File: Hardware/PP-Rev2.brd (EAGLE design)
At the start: 190.5 x 101.3 mm, 181 parts, among them IC1 LT6004, IC2 TLC6C5912-Q1, J1 J_0399700102, Q1 MOSFET-PCHANNEL, Q10 2N7002PW, Q11 2N7002PW, Q12 2N7002PW, Q13 2N7002PW, Q14 2N7002PW, Q15 2N7002PW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

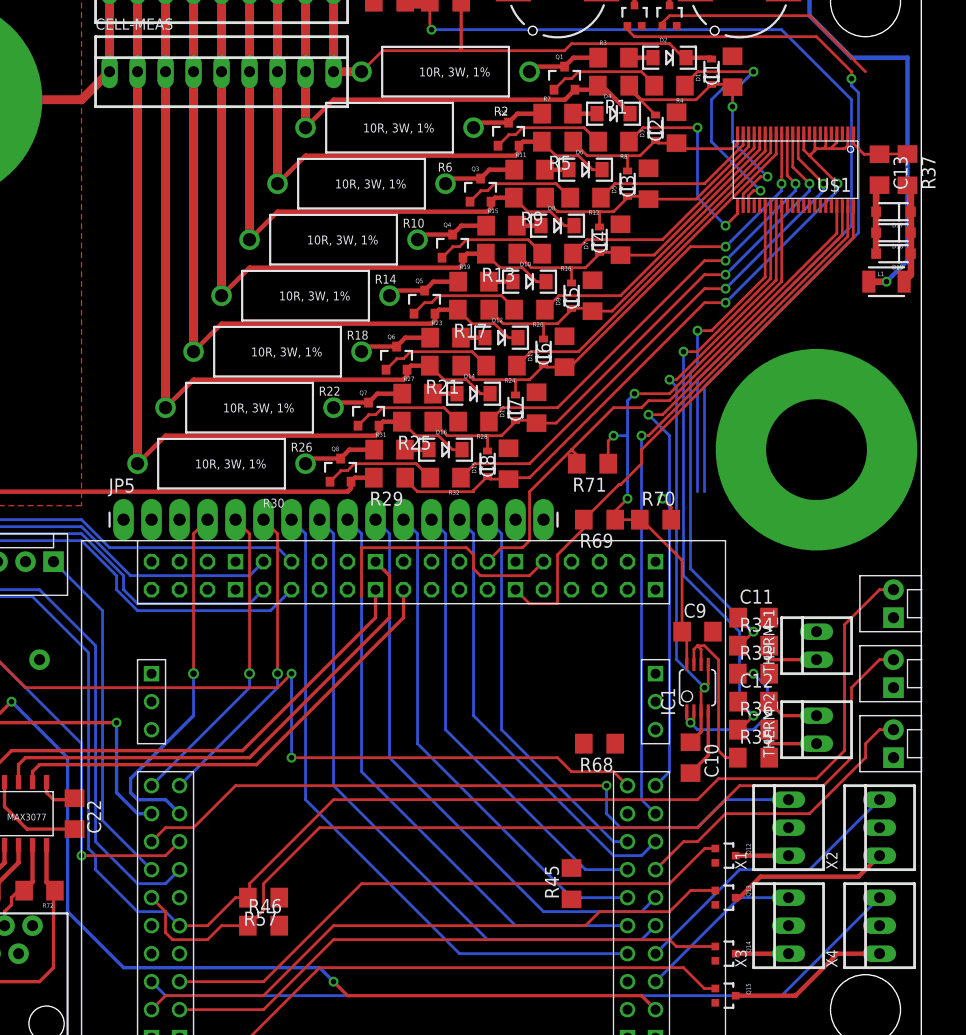
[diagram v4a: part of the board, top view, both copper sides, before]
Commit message: Pretty much all signal traces routed
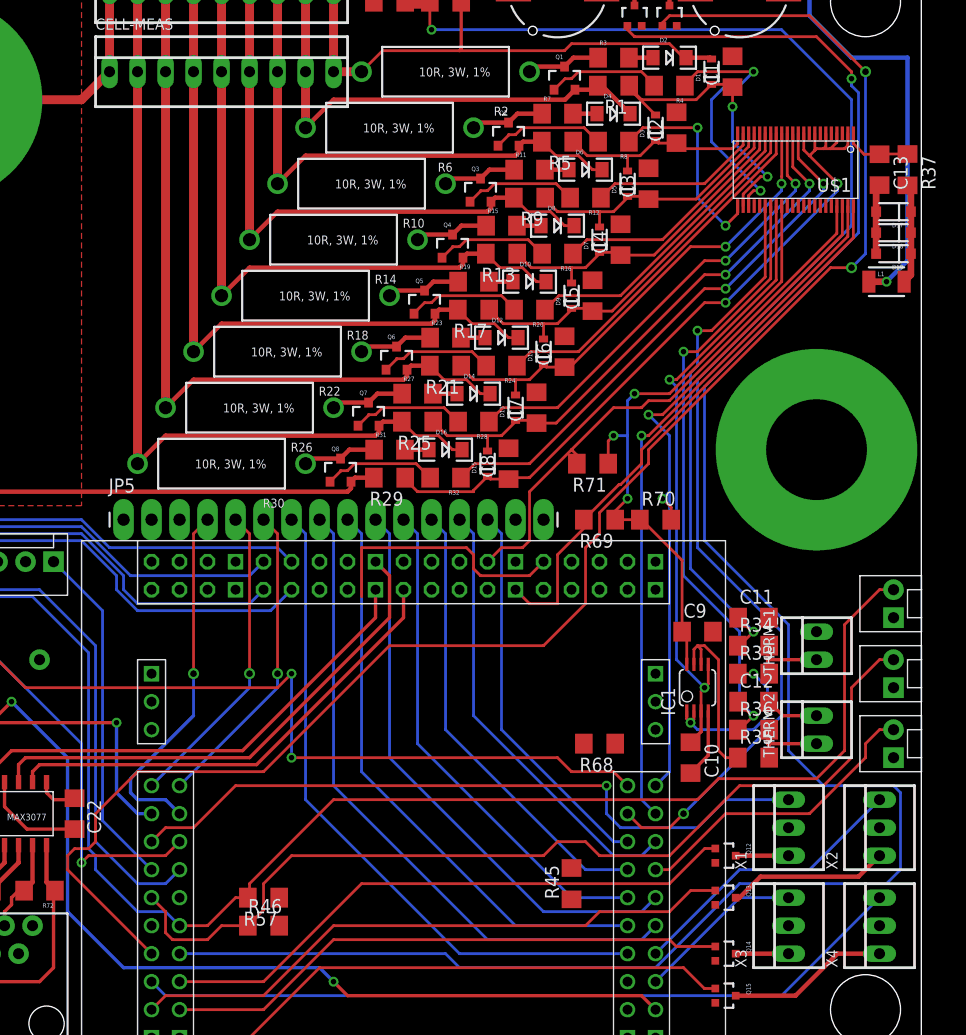
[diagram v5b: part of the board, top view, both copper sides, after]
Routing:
- net BUZZ_2: track 21.1 -> 151.0 mm, vias 0 -> 2
- net BUZZ_1: track 66.4 -> 181.4 mm
- net V_CHECK_OUT: track 86.9 -> 129.1 mm, vias 1 -> 2
- net ESTOP_2: track 85.6 -> 86.7 mm
- net V_CHECK_CHARGER_IN: track 38.3 -> 39.2 mm
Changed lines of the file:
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@@
 <wire x1="184.15" y1="87.63" x2="184.15" y2="76.2" width="0.254" layer="16"/>
 <wire x1="184.15" y1="76.2" x2="170.18" y2="62.23" width="0.254" layer="16"/>
-<wire x1="170.18" y1="62.23" x2="170.18" y2="52.07" width="0.254" layer="16"/>
-<wire x1="170.18" y1="52.07" x2="163.83" y2="22.86" width="0" layer="19" extent="16-16"/>
+<wire x1="170.18" y1="62.23" x2="170.18" y2="46.99" width="0.254" layer="16"/>
+<wire x1="170.18" y1="46.99" x2="177.8" y2="39.37" width="0.254" layer="16"/>
+<wire x1="163.83" y1="22.86" x2="165.1" y2="21.59" width="0.254" layer="1"/>
+<wire x1="165.1" y1="21.59" x2="167.64" y2="21.59" width="0.254" layer="1"/>
+<wire x1="167.64" y1="21.59" x2="168.91" y2="22.86" width="0.254" layer="1"/>
+<via x="168.91" y="22.86" extent="1-16" drill="0.6"/>
+<wire x1="168.91" y1="22.86" x2="177.8" y2="31.75" width="0.254" layer="16"/>
+<wire x1="177.8" y1="31.75" x2="177.8" y2="39.37" width="0.254" layer="16"/>
 </signal>
 <signal name="N$36">
@@
 <contactref element="U$13" pad="5.1"/>
 <wire x1="123.19" y1="20.32" x2="121.92" y2="19.05" width="0.254" layer="1"/>
-<wire x1="121.92" y1="19.05" x2="114.3" y2="19.05" width="0.254" layer="1"/>
-<via x="114.3" y="19.05" extent="1-16" drill="0.5"/>
-<wire x1="114.3" y1="19.05" x2="114.3" y2="29.21" width="0.254" layer="16"/>
+<wire x1="121.92" y1="19.05" x2="115.57" y2="19.05" width="0.254" layer="1"/>
+<wire x1="115.57" y1="19.05" x2="114.935" y2="19.05" width="0.254" layer="1"/>
+<wire x1="114.935" y1="19.05" x2="114.3" y2="18.415" width="0.254" layer="1"/>
+<via x="114.3" y="18.415" extent="1-16" drill="0.5"/>
+<wire x1="114.3" y1="18.415" x2="114.3" y2="29.21" width="0.254" layer="16"/>
 <wire x1="114.3" y1="29.21" x2="106.68" y2="36.83" width="0.254" layer="16"/>
 <wire x1="106.68" y1="36.83" x2="102.87" y2="36.83" width="0.254" layer="16"/>
@@
 <wire x1="185.42" y1="27.94" x2="180.34" y2="22.86" width="0.254" layer="1"/>
 <wire x1="180.34" y1="22.86" x2="172.72" y2="22.86" width="0.254" layer="1"/>
-<wire x1="172.72" y1="22.86" x2="170.18" y2="20.32" width="0.254" layer="1"/>
-<wire x1="170.18" y1="20.32" x2="168.91" y2="20.32" width="0.254" layer="1"/>
-<wire x1="168.91" y1="20.32" x2="166.37" y2="17.78" width="0.254" layer="1"/>
+<wire x1="172.72" y1="22.86" x2="167.64" y2="17.78" width="0.254" layer="1"/>
+<wire x1="167.64" y1="17.78" x2="166.37" y2="17.78" width="0.254" layer="1"/>
 <wire x1="158.75" y1="15.088" x2="166.37" y2="17.78" width="0" layer="19" extent="1-1"/>
 </signal>
@@
 <wire x1="184.15" y1="27.94" x2="181.61" y2="25.4" width="0.254" layer="1"/>
 <wire x1="181.61" y1="25.4" x2="173.99" y2="25.4" width="0.254" layer="1"/>
-<wire x1="173.99" y1="25.4" x2="170.18" y2="21.59" width="0.254" layer="1"/>
-<wire x1="170.18" y1="21.59" x2="135.89" y2="21.59" width="0.254" layer="1"/>
-<wire x1="135.89" y1="21.59" x2="130.81" y2="16.51" width="0.254" layer="1"/>
+<wire x1="173.99" y1="25.4" x2="167.64" y2="19.05" width="0.254" layer="1"/>
+<wire x1="167.64" y1="19.05" x2="161.29" y2="19.05" width="0.254" layer="1"/>
+<wire x1="161.29" y1="19.05" x2="160.02" y2="20.32" width="0.254" layer="1"/>
+<wire x1="160.02" y1="20.32" x2="157.48" y2="20.32" width="0.254" layer="1"/>
+<wire x1="157.48" y1="20.32" x2="156.21" y2="19.05" width="0.254" layer="1"/>
+<wire x1="156.21" y1="19.05" x2="133.35" y2="19.05" width="0.254" layer="1"/>
+<wire x1="133.35" y1="19.05" x2="130.81" y2="16.51" width="0.254" layer="1"/>
 <wire x1="130.81" y1="16.51" x2="130.81" y2="14.122" width="0.254" layer="1"/>
 <wire x1="130.81" y1="14.122" x2="129.388" y2="12.7" width="0.254" layer="1"/>
@@
 <wire x1="167.64" y1="95.25" x2="180.34" y2="95.25" width="0.254" layer="1"/>
 <wire x1="180.34" y1="95.25" x2="185.42" y2="90.17" width="0.254" layer="1"/>
-<wire x1="166.99" y1="94.325" x2="120.65" y2="10.16" width="0" layer="19" extent="1-1"/>
+<via x="185.42" y="90.17" extent="1-16" drill="0.6"/>
+<wire x1="185.42" y1="90.17" x2="185.42" y2="73.66" width="0.254" layer="16"/>
+<wire x1="185.42" y1="73.66" x2="184.15" y2="72.39" width="0.254" layer="16"/>
+<via x="184.15" y="72.39" extent="1-16" drill="0.6"/>
+<wire x1="184.15" y1="72.39" x2="182.245" y2="72.39" width="0.254" layer="1"/>
+<wire x1="182.245" y1="72.39" x2="165.735" y2="55.88" width="0.254" layer="1"/>
+<wire x1="165.735" y1="55.88" x2="165.735" y2="54.61" width="0.254" layer="1"/>
+<wire x1="165.735" y1="54.61" x2="161.29" y2="50.165" width="0.254" layer="1"/>
+<wire x1="161.29" y1="50.165" x2="161.29" y2="48.26" width="0.254" layer="1"/>
+<wire x1="161.29" y1="48.26" x2="160.02" y2="46.99" width="0.254" layer="1"/>
+<wire x1="160.02" y1="46.99" x2="160.02" y2="41.91" width="0.254" layer="1"/>
+<wire x1="160.02" y1="41.91" x2="156.21" y2="38.1" width="0.254" layer="1"/>
+<wire x1="156.21" y1="38.1" x2="142.24" y2="38.1" width="0.254" layer="1"/>
+<wire x1="142.24" y1="38.1" x2="130.81" y2="26.67" width="0.254" layer="1"/>
+<wire x1="130.81" y1="26.67" x2="119.38" y2="26.67" width="0.254" layer="1"/>
+<wire x1="119.38" y1="26.67" x2="115.57" y2="22.86" width="0.254" layer="1"/>
+<wire x1="115.57" y1="22.86" x2="115.57" y2="20.32" width="0.254" layer="1"/>
+<wire x1="115.57" y1="20.32" x2="114.935" y2="19.685" width="0.254" layer="1"/>
+<wire x1="114.935" y1="19.685" x2="113.665" y2="19.685" width="0.254" layer="1"/>
+<wire x1="113.665" y1="19.685" x2="113.03" y2="19.05" width="0.254" layer="1"/>
+<wire x1="113.03" y1="19.05" x2="113.03" y2="17.78" width="0.254" layer="1"/>
+<wire x1="113.03" y1="17.78" x2="120.65" y2="10.16" width="0.254" layer="1"/>
 </signal>
 <signal name="BUZZ_1">
@@
 <wire x1="184.785" y1="88.265" x2="184.785" y2="75.565" width="0.254" layer="16"/>
 <wire x1="184.785" y1="75.565" x2="170.815" y2="61.595" width="0.254" layer="16"/>
-<wire x1="170.815" y1="61.595" x2="170.815" y2="52.07" width="0.254" layer="16"/>
-<wire x1="170.815" y1="52.07" x2="123.19" y2="10.16" width="0" layer="19" extent="16-16"/>
+<wire x1="170.815" y1="61.595" x2="170.815" y2="47.625" width="0.254" layer="16"/>
+<wire x1="170.815" y1="47.625" x2="178.435" y2="40.005" width="0.254" layer="16"/>
+<wire x1="178.435" y1="40.005" x2="178.435" y2="28.575" width="0.254" layer="16"/>
+<wire x1="178.435" y1="28.575" x2="181.61" y2="25.4" width="0.254" layer="16"/>
+<wire x1="123.19" y1="10.16" x2="147.32" y2="10.16" width="0.254" layer="16"/>
+<wire x1="147.32" y1="10.16" x2="148.59" y2="8.89" width="0.254" layer="16"/>
+<wire x1="148.59" y1="8.89" x2="166.37" y2="8.89" width="0.254" layer="16"/>
+<wire x1="166.37" y1="8.89" x2="173.99" y2="16.51" width="0.254" layer="16"/>
+<wire x1="173.99" y1="16.51" x2="187.325" y2="16.51" width="0.254" layer="16"/>
+<wire x1="187.325" y1="16.51" x2="188.595" y2="17.78" width="0.254" layer="16"/>
+<wire x1="188.595" y1="17.78" x2="188.595" y2="24.765" width="0.254" layer="16"/>
+<wire x1="188.595" y1="24.765" x2="187.96" y2="25.4" width="0.254" layer="16"/>
+<wire x1="187.96" y1="25.4" x2="181.61" y2="25.4" width="0.254" layer="16"/>
 </signal>
 <signal name="GAUGE_ON">

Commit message: Lots of power supply routing. Merged two independent 5V supplies into one supply
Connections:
- removed net +5V: C22.1, U$15.VCC, U$2.1, U$4.1
- net 5V: now also C22.1, U$15.VCC, U$2.1, U$4.1
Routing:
- net 5V: track 0.00 -> 477.9 mm, vias 0 -> 9
- net +12V: track 4.94 -> 355.6 mm, vias 0 -> 5
- net +3V3: track 0.00 -> 184.4 mm, vias 0 -> 4
- net V_CHECK_ARRAY: track 25.5 -> 108.1 mm
- net CHARGER+: track 0.00 -> 34.0 mm, vias 0 -> 1
- net LOGIC_POWER: track 0.00 -> 31.0 mm
- net LCD_VBACK: track 0.00 -> 19.4 mm
- net N$41: track 9.04 -> 25.6 mm
- net GND: track 85.0 -> 96.9 mm
- net ESTOP_1: track 27.6 -> 36.3 mm
- net N$33: track 0.00 -> 8.61 mm
- net N$100: track 0.00 -> 6.57 mm
- net N$42: track 0.00 -> 4.21 mm
- net V_CHECK_CHARGER_IN: track 39.2 -> 43.1 mm
- net +5V: track 3.81 -> 0.00 mm
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
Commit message: All signals routed except GND
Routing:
- net 5V: track 477.9 -> 633.7 mm, vias 9 -> 16
- net N$41: track 25.6 -> 48.0 mm
- net GND: track 96.9 -> 103.2 mm
- net BUZZ_1: track 181.4 -> 181.9 mm
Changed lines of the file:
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@@
 <wire x1="39.37" y1="80.01" x2="43.18" y2="80.01" width="1.778" layer="1"/>
 <contactref element="C22" pad="2"/>
+<wire x1="109.35" y1="21.46" x2="113.665" y2="21.46" width="0.3048" layer="1"/>
 <wire x1="178.32" y1="77.98" x2="175.32" y2="77.98" width="0" layer="19" extent="1-1"/>
 <wire x1="179.82" y1="77.98" x2="178.32" y2="77.98" width="0" layer="19" extent="1-1"/>
@@
 <wire x1="168.91" y1="91.44" x2="168.275" y2="86.49" width="0" layer="19" extent="1-1"/>
 <wire x1="168.29" y1="94.325" x2="167.64" y2="92.71" width="0" layer="19" extent="1-1"/>
-<wire x1="173.355" y1="91.57" x2="171.45" y2="91.32" width="0" layer="19" extent="1-1"/>
 <wire x1="165.115" y1="94.325" x2="167.64" y2="92.71" width="0" layer="19" extent="1-1"/>
 <wire x1="180.975" y1="55.88" x2="186.385" y2="73.66" width="0" layer="19" extent="1-1"/>
@@
 <wire x1="97.79" y1="29.15" x2="96.368" y2="38.1" width="0" layer="19" extent="1-1"/>
 <wire x1="107.315" y1="25.7175" x2="97.79" y2="29.15" width="0" layer="19" extent="1-1"/>
-<wire x1="113.665" y1="21.46" x2="109.35" y2="21.46" width="0" layer="19" extent="1-1"/>
 <wire x1="109.855" y1="12.7" x2="109.35" y2="21.46" width="0" layer="19" extent="1-1"/>
 <wire x1="108.585" y1="10.16" x2="109.855" y2="12.7" width="0" layer="19" extent="1-1"/>
@@
 <wire x1="34.42" y1="93.345" x2="38.1" y2="82.42" width="0" layer="19" extent="1-1"/>
 <wire x1="45.72" y1="96.52" x2="34.42" y2="96.39" width="0" layer="19" extent="1-1"/>
+<wire x1="171.45" y1="91.32" x2="173.105" y2="91.32" width="0.6096" layer="1"/>
+<wire x1="173.105" y1="91.32" x2="173.355" y2="91.57" width="0.6096" layer="1"/>
 </signal>
 <signal name="N$2">
@@
 <contactref element="U$4" pad="1"/>
 <contactref element="U$2" pad="1"/>
-<wire x1="177.99" y1="97.79" x2="153.48" y2="97.79" width="0" layer="19" extent="1-1"/>
-<wire x1="113.03" y1="99.06" x2="153.48" y2="97.79" width="0" layer="19" extent="1-16"/>
-<wire x1="111.125" y1="25.7175" x2="111.125" y2="34.925" width="0" layer="19" extent="1-1"/>
-<wire x1="113.665" y1="24.26" x2="111.125" y2="25.7175" width="0" layer="19" extent="1-1"/>
-<wire x1="86.99" y1="34.29" x2="105.41" y2="34.29" width="0" layer="19" extent="1-1"/>
-<wire x1="48.89" y1="34.29" x2="86.99" y2="34.29" width="0" layer="19" extent="1-1"/>
+<wire x1="105.41" y1="34.29" x2="102.87" y2="34.29" width="0.4064" layer="1"/>
+<wire x1="102.87" y1="34.29" x2="101.6" y2="33.02" width="0.4064" layer="1"/>
+<wire x1="101.6" y1="33.02" x2="88.26" y2="33.02" width="0.4064" layer="1"/>
+<wire x1="88.26" y1="33.02" x2="86.99" y2="34.29" width="0.4064" layer="1"/>
+<wire x1="86.99" y1="34.29" x2="86.99" y2="34.93" width="0.4064" layer="1"/>
+<wire x1="86.99" y1="34.93" x2="81.28" y2="40.64" width="0.4064" layer="1"/>
+<via x="81.28" y="40.64" extent="1-16" drill="0.5"/>
+<wire x1="81.28" y1="40.64" x2="67.31" y2="40.64" width="0.4064" layer="16"/>
+<via x="67.31" y="40.64" extent="1-16" drill="0.5"/>
+<wire x1="67.31" y1="40.64" x2="52.07" y2="40.64" width="0.4064" layer="1"/>
+<wire x1="52.07" y1="40.64" x2="48.89" y2="37.46" width="0.4064" layer="1"/>
+<wire x1="48.89" y1="37.46" x2="48.89" y2="34.29" width="0.4064" layer="1"/>
+<wire x1="111.76" y1="24.13" x2="113.535" y2="24.13" width="0.3048" layer="1"/>
+<wire x1="113.535" y1="24.13" x2="113.665" y2="24.26" width="0.3048" layer="1"/>
+<wire x1="111.125" y1="25.7175" x2="111.125" y2="24.765" width="0.3048" layer="1"/>
+<wire x1="111.125" y1="24.765" x2="111.76" y2="24.13" width="0.3048" layer="1"/>
+<wire x1="111.76" y1="24.13" x2="111.76" y2="26.035" width="0.3048" layer="1"/>
+<via x="111.76" y="26.035" extent="1-16" drill="0.5"/>
+<wire x1="111.76" y1="26.035" x2="111.76" y2="27.94" width="0.3048" layer="16"/>
+<wire x1="111.76" y1="27.94" x2="105.41" y2="34.29" width="0.3048" layer="16"/>
+<via x="113.03" y="99.06" extent="1-16" drill="0.6"/>
+<wire x1="113.03" y1="99.06" x2="113.03" y2="96.52" width="0.6096" layer="1"/>
+<wire x1="113.03" y1="96.52" x2="115.57" y2="93.98" width="0.6096" layer="1"/>
+<via x="115.57" y="93.98" extent="1-16" drill="0.6"/>
+<wire x1="115.57" y1="93.98" x2="138.43" y2="93.98" width="0.6096" layer="16"/>
+<wire x1="138.43" y1="93.98" x2="142.24" y2="97.79" width="0.6096" layer="16"/>
+<wire x1="142.24" y1="97.79" x2="150.495" y2="97.79" width="0.6096" layer="16"/>
+<via x="150.495" y="97.79" extent="1-16" drill="0.6"/>
+<wire x1="150.495" y1="97.79" x2="153.48" y2="97.79" width="0.6096" layer="1"/>
+<wire x1="177.99" y1="97.79" x2="176.53" y2="97.79" width="0.6096" layer="1"/>
+<wire x1="176.53" y1="97.79" x2="175.26" y2="96.52" width="0.6096" layer="1"/>
+<via x="175.26" y="96.52" extent="1-16" drill="0.6"/>
+<wire x1="175.26" y1="96.52" x2="151.765" y2="96.52" width="0.6096" layer="16"/>
+<wire x1="151.765" y1="96.52" x2="150.495" y2="97.79" width="0.6096" layer="16"/>
 </signal>
 <signal name="ESTOP_1">
@@
 <wire x1="53.34" y1="69.85" x2="55.88" y2="69.85" width="1.778" layer="1"/>
 <wire x1="55.88" y1="69.85" x2="57.15" y2="68.58" width="1.778" layer="1"/>
-<wire x1="66.675" y1="48.32" x2="69.215" y2="48.32" width="0" layer="19" extent="1-1"/>
-<wire x1="64.77" y1="47.12" x2="66.675" y2="48.32" width="0" layer="19" extent="1-1"/>
-<wire x1="78.105" y1="49.047" x2="69.215" y2="48.32" width="0" layer="19" extent="1-1"/>
+<wire x1="66.675" y1="48.32" x2="66.675" y2="47.625" width="0.6096" layer="1"/>
+<wire x1="66.675" y1="47.625" x2="66.04" y2="46.99" width="0.6096" layer="1"/>
+<wire x1="66.04" y1="46.99" x2="64.9" y2="46.99" width="0.6096" layer="1"/>
+<wire x1="64.9" y1="46.99" x2="64.77" y2="47.12" width="0.6096" layer="1"/>
+<wire x1="66.675" y1="48.32" x2="66.675" y2="46.99" width="0.6096" layer="1"/>
+<wire x1="66.675" y1="46.99" x2="67.31" y2="46.355" width="0.6096" layer="1"/>
+<wire x1="67.31" y1="46.355" x2="68.58" y2="46.355" width="0.6096" layer="1"/>
+<wire x1="68.58" y1="46.355" x2="69.215" y2="46.99" width="0.6096" layer="1"/>
+<wire x1="69.215" y1="46.99" x2="69.215" y2="48.32" width="0.6096" layer="1"/>
+<wire x1="69.215" y1="48.32" x2="69.215" y2="53.975" width="0.6096" layer="1"/>
+<wire x1="69.215" y1="53.975" x2="63.5" y2="59.69" width="0.6096" layer="1"/>
 </signal>
 <signal name="N$42">
@@
 <wire x1="163.815" y1="94.325" x2="163.815" y2="93.995" width="0.254" layer="1"/>
 <wire x1="163.815" y1="93.995" x2="164.465" y2="93.345" width="0.254" layer="1"/>
-<wire x1="164.465" y1="93.345" x2="180.975" y2="93.345" width="0.254" layer="1"/>
+<wire x1="164.465" y1="93.345" x2="170.815" y2="93.345" width="0.254" layer="1"/>
+<wire x1="170.815" y1="93.345" x2="171.45" y2="92.71" width="0.254" layer="1"/>
+<wire x1="171.45" y1="92.71" x2="172.085" y2="92.71" width="0.254" layer="1"/>
+<wire x1="172.085" y1="92.71" x2="172.72" y2="93.345" width="0.254" layer="1"/>
+<wire x1="172.72" y1="93.345" x2="180.975" y2="93.345" width="0.254" layer="1"/>
 <wire x1="180.975" y1="93.345" x2="184.15" y2="90.17" width="0.254" layer="1"/>
 <wire x1="184.15" y1="90.17" x2="184.15" y2="89.535" width="0.254" layer="1"/>
@@
 <wire x1="112.395" y1="6.985" x2="111.76" y2="6.985" width="0.3048" layer="1"/>
 <via x="111.76" y="6.985" extent="1-16" drill="0.6"/>
-<wire x1="111.76" y1="6.985" x2="111.76" y2="26.67" width="0.3048" layer="16"/>
-<wire x1="111.76" y1="26.67" x2="106.68" y2="31.75" width="0.3048" layer="16"/>
+<wire x1="111.76" y1="6.985" x2="111.76" y2="13.97" width="0.3048" layer="16"/>
+<wire x1="111.76" y1="13.97" x2="109.22" y2="16.51" width="0.3048" layer="16"/>
+<wire x1="109.22" y1="16.51" x2="109.22" y2="29.21" width="0.3048" layer="16"/>
+<wire x1="109.22" y1="29.21" x2="106.68" y2="31.75" width="0.3048" layer="16"/>
 <wire x1="106.68" y1="31.75" x2="102.87" y2="31.75" width="0.3048" layer="16"/>
 <wire x1="102.87" y1="31.75" x2="100.33" y2="34.29" width="0.3048" layer="16"/>
